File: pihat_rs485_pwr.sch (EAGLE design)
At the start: 39 parts, among them IC1 MAX481CSA, Q1 MOSFET-N2N7002, Q2 MOSFET-N2N7002, Q3 MOSFET-N2N7002

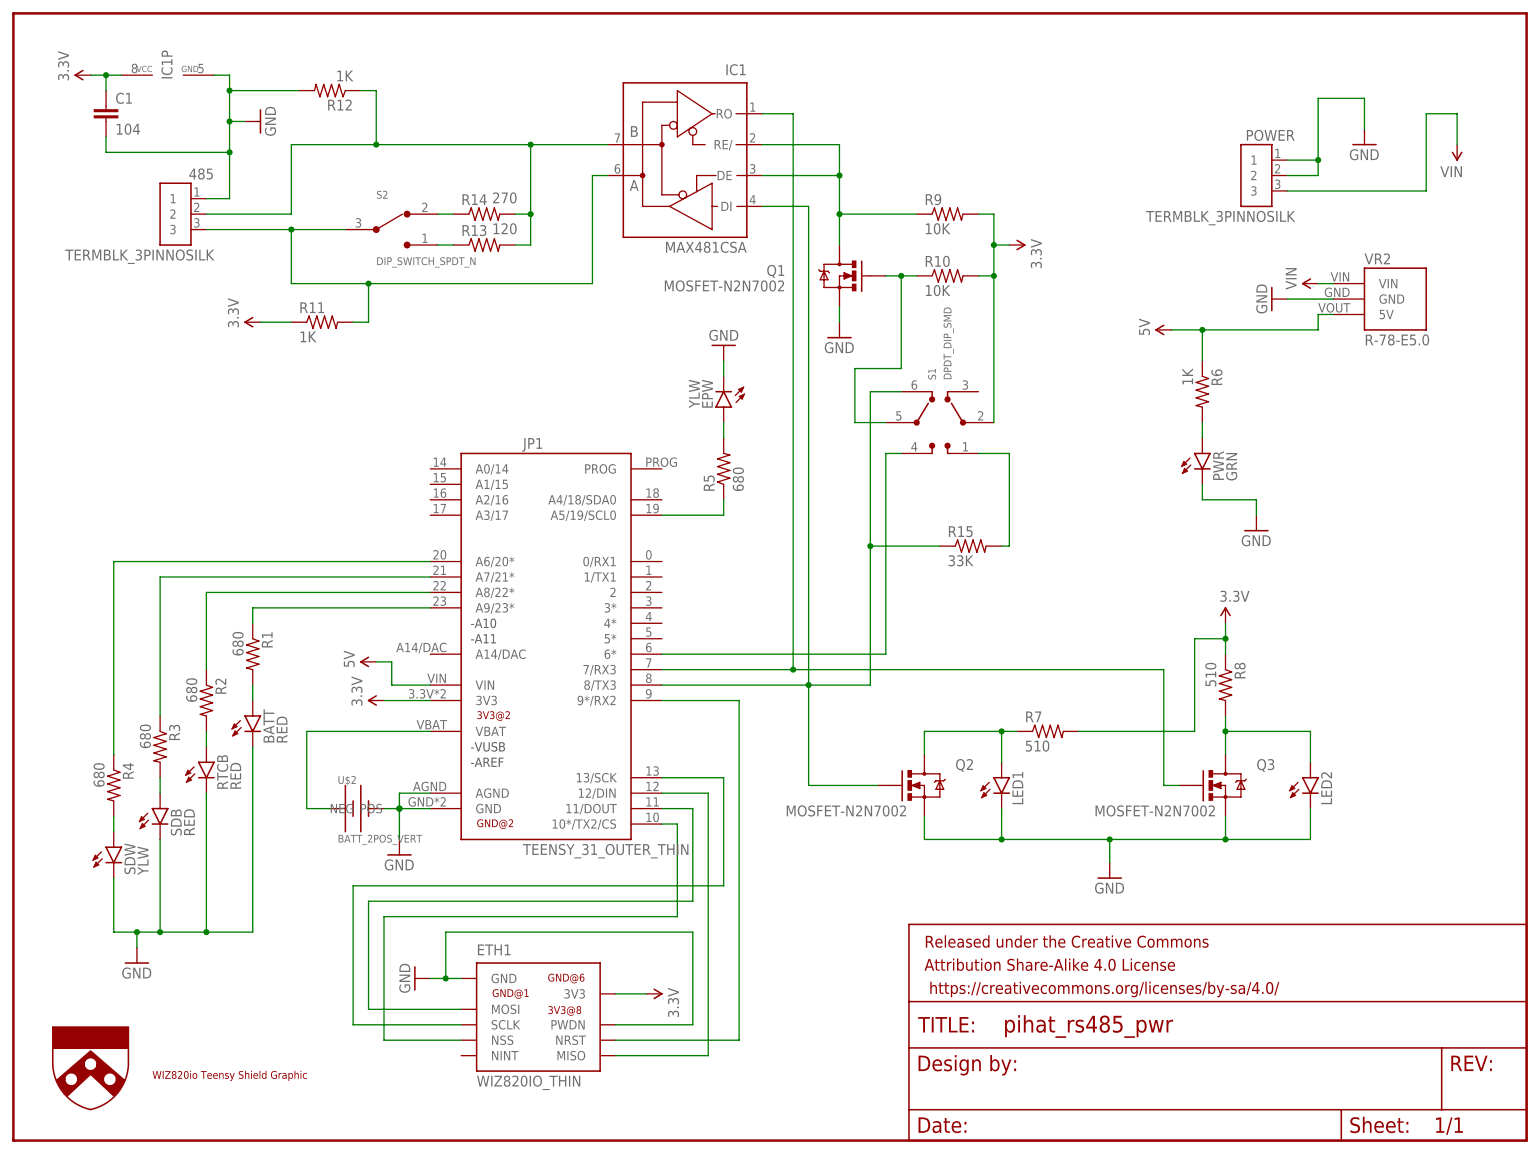
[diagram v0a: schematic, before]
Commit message: 10/9/17, removed teensy, changed board dims
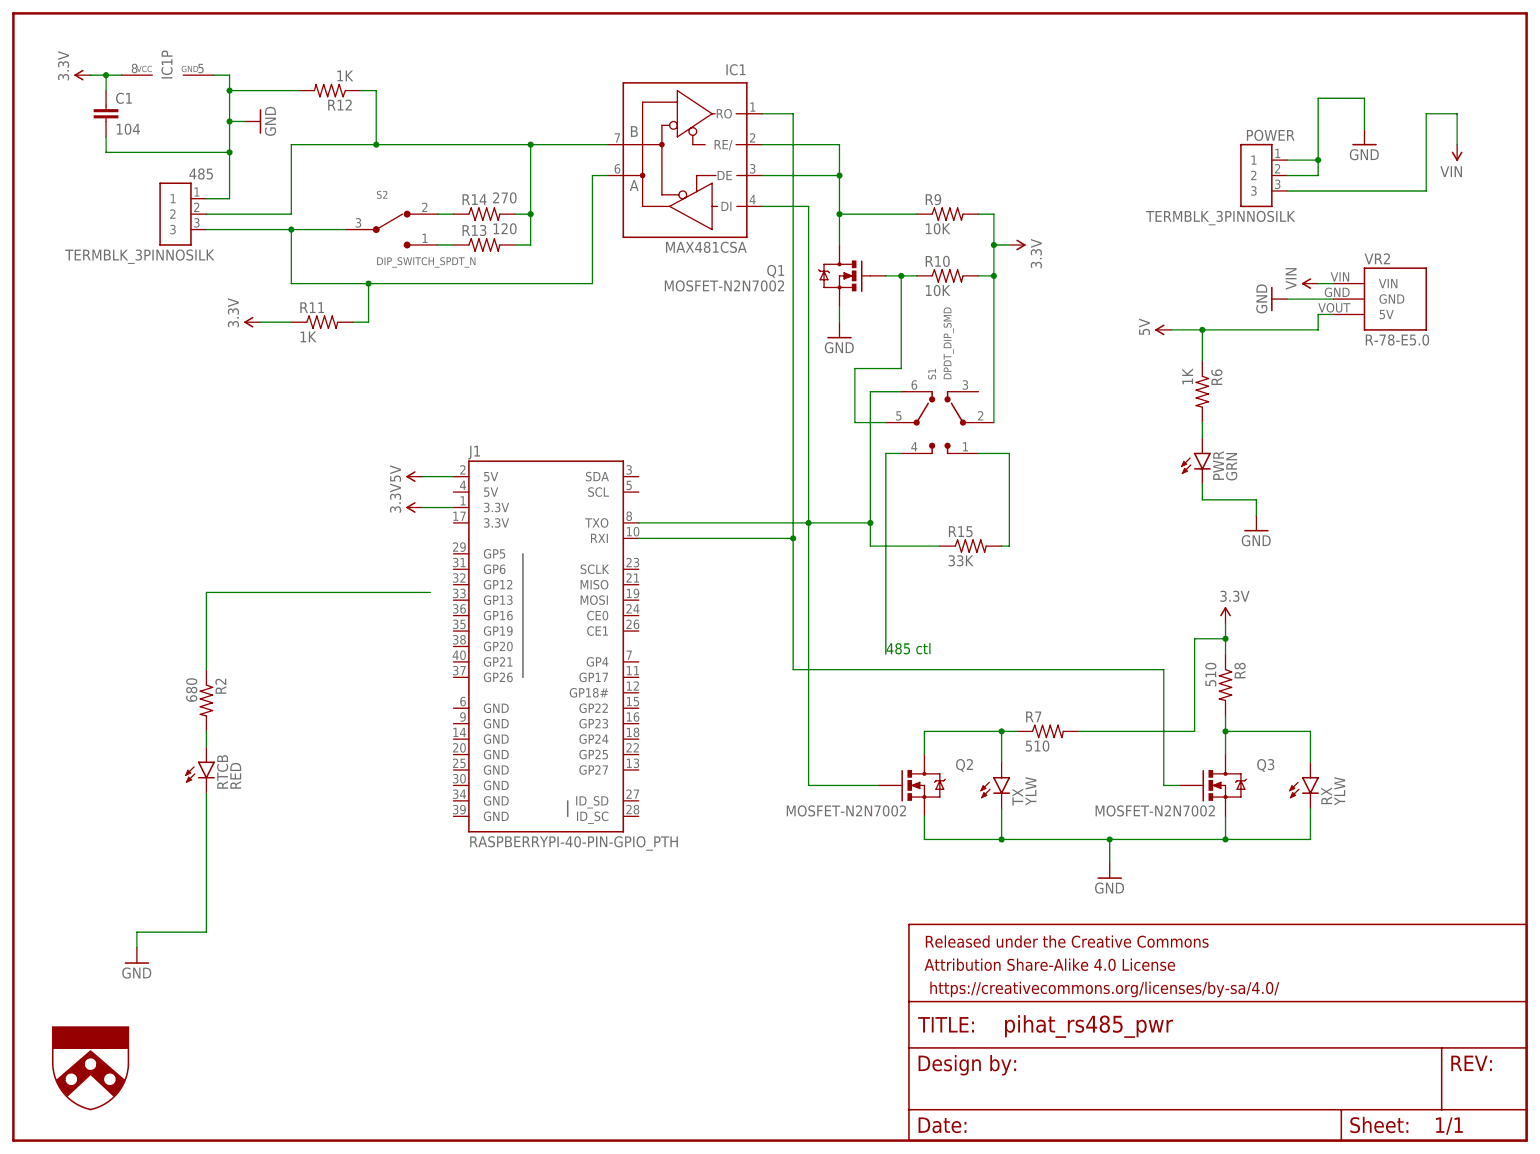
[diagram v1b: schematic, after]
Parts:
- removed BATT, SDB: RED, SparkFun-LED:LED0603
- removed EPW, SDW: YLW, SparkFun-LED:LED0603
- removed ETH1: WIZ820IO_THIN, UPenn:WIZ820IO_THIN
- removed JP1: TEENSY_31_OUTER_THIN, UPenn:TEENSY_31_OUTER_THIN
- removed R1, R3, R4, R5: 680, SparkFun-Resistors:RESISTOR0603
- removed U$1: WIZ820_SHLD_OVRLY, UPenn:WIZ820_SHLD_OVRLY
- removed U$2: BATT_2POS_VERT, UPenn:BATT_2POS_VERT
- added J1: RASPBERRYPI-40-PIN-GPIO_PTH, SparkFun-Connectors:RASPBERRYPI-40-PIN-GPIO_PTH
- RX, TX: value (none) -> YLW
- renumbered LED1 to TX, LED2 to RX
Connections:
- removed net N$10: ETH1.NRST, JP1.9*/RX2
- removed net N$11: EPW.A, R5.2
- removed net N$18: BATT.A, R1.2
- removed net N$19: R3.2, SDB.A
- removed net N$21: R4.2, SDW.A
- removed net N$23: JP1.A7/21*, R3.1
- removed net N$24: JP1.A6/20*, R4.1
- removed net N$3: JP1.VBAT, U$2.POS
- removed net N$4: JP1.A5/19/SCL0, R5.1
- removed net N$5: ETH1.NSS, JP1.10*/TX2/CS
- removed net N$6: ETH1.MOSI, JP1.11/DOUT
- removed net N$7: ETH1.MISO, JP1.12/DIN
- removed net N$8: ETH1.SCLK, JP1.13/SCK
- removed net N$9: JP1.A9/23*, R1.1
- net 3.3V: now also J1.3.3V@1; no longer ETH1.3V3@7, JP1.3V3@1
- net 5V: now also J1.5V@2; no longer JP1.VIN
- net GND: no longer BATT.C, EPW.C, ETH1.GND@0, ETH1.PWDN, JP1.AGND, JP1.GND@1, SDB.C, SDW.C, U$2.NEG
- net N$16: no longer JP1.7/RX3
- net N$17: no longer JP1.8/TX3
- net N$2: no longer JP1.6*
- net N$22: no longer JP1.A8/22*
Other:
- note added: "485 ctl"

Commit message: 10/16/17, mostly set
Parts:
- removed VR2: R-78-E5.0, UPenn:R-78-E5.0
- added C2: 1.0 uF, resistor:C-USC0603
- added C3: 47 uF, resistor:C-USC0603
- added R1: 10K, SparkFun-Resistors:RESISTOR0603
- added R3: 47K, SparkFun-Resistors:RESISTOR0603
- added U$1: MOSFET-P_SMD, UPenn:MOSFET-P_SMD
- added U$2: FUSE, UPenn:FUSE
- added U$3: BIPOLAR_TRANS_ARRAY, UPenn:BIPOLAR_TRANS_ARRAY
- added U$5: DIODE_UNI, UPenn:DIODE_UNI
- added VR1: D24V22F5, UPenn:D24V22F5
- C1: value 104 -> 0.1uF; device SparkFun-Capacitors:CAP0603-CAP -> resistor:C-USC0603
- J1: value RASPBERRYPI-40-PIN-GPIO_PTH -> RASPBERRYPI-40-PIN-GPIO_PTH_NO_SHROUND; device SparkFun-Connectors:RASPBERRYPI-40-PIN-GPIO_PTH -> UPenn:RASPBERRYPI-40-PIN-GPIO_PTH_NO_SHROUND
- R14: value 270 -> 180
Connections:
- removed net N$17: IC1G$1.DI, Q2.G, R15.1, S1.6>
- new net N$3: IC1G$1.DI, J1.TXO, Q2.G, R15.1, S1.6>
- new net N$4: R1.2, U$3.P$2, U$3.P$5, U$3.P$6
- new net N$5: R3.2, U$1.G, U$3.P$3
- new net N$7: C2.1, U$1.D, U$2.P$2, U$3.P$1
- new net N$8: U$2.P$1, VR1.5V
- net 5V: now also C3.1, U$1.S, U$3.P$4, U$5.CA; no longer VR2.5V
- net GND: now also C2.2, C3.2, J1.GND@6, R1.1, R3.1, U$5.AN, VR1.GND; no longer VR2.GND
- net N$16: now also J1.RXI
- net N$2: now also J1.GP22
- net VIN: now also VR1.VIN; no longer VR2.VIN
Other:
- note added: "POWER"
- note removed: "485 ctl"
- moved on the sheet: J1, POWER, Q1, Q2, Q3, R10, R11, R15, R2, R6, R7, R8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

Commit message: 10/16/17, all silkscreens placed
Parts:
- renumbered IC1 to U1, U$1 to Q4, U$2 to F1, U$3 to Q5, U$5 to D1, VR1 to PS1
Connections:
- net N$22: now also J1.GP17
